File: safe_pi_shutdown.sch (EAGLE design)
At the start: 31 parts, among them U1 LTC2952CF

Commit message: prawie pierwsza wersja
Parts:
- added J1: 22-27-2021-02, con-molex:22-27-2021-02
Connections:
- removed net N$7: S1.2.1, U1.!PB
- new net N$5: J1-1.S, S1.2.1, S1.2.2, U1.!PB
- net GND: now also J1-2.S, X2.1; no longer X2.2
- net V1: now also X2.2; no longer X2.1
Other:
- moved on the sheet: X2
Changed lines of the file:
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@@
 <?xml version="1.0" encoding="utf-8"?>
 <!DOCTYPE eagle SYSTEM "eagle.dtd">
-<eagle version="6.5.0">
+<eagle version="6.6.0">
 <drawing>
 <settings>
@@
 <classes>
 <class number="0" name="default" width="0.2032" drill="0.6096">
-<clearance class="0" value="0.2032"/>
+<clearance class="0" value="0.205"/>
 </class>
 <class number="1" name="VCC" width="0.508" drill="0.6096">
-<clearance class="1" value="0.2032"/>
+<clearance class="0" value="0.205"/>
+<clearance class="1" value="0.205"/>
 </class>
 </classes>
@@
 <part name="U$2" library="mcp73831" deviceset="MCP73831" device=""/>
 <part name="SUPPLY14" library="supply2" deviceset="GND" device=""/>
+<part name="J1" library="con-molex" deviceset="22-?-02" device="27-2021"/>
 </parts>
 <sheets>
@@
 <instance part="SUPPLY3" gate="GND" x="38.1" y="154.94" rot="R180"/>
 <instance part="SUPPLY6" gate="GND" x="50.8" y="121.92"/>
-<instance part="X2" gate="G$1" x="25.4" y="127"/>
+<instance part="X2" gate="G$1" x="27.94" y="124.46" rot="MR180"/>
 <instance part="C7" gate="G$1" x="162.56" y="144.78"/>
 <instance part="C8" gate="G$1" x="220.98" y="160.02"/>
@@
 <instance part="U$2" gate="G$1" x="22.86" y="139.7" rot="MR180"/>
 <instance part="SUPPLY14" gate="GND" x="10.16" y="124.46"/>
+<instance part="J1" gate="-1" x="91.44" y="81.28"/>
+<instance part="J1" gate="-2" x="91.44" y="78.74"/>
 </instances>
 <busses>
@@
 <pinref part="SUPPLY6" gate="GND" pin="GND"/>
 <wire x1="50.8" y1="127" x2="50.8" y2="124.46" width="0.1524" layer="91"/>
-<pinref part="X2" gate="G$1" pin="2"/>
-<wire x1="33.02" y1="124.46" x2="50.8" y2="124.46" width="0.1524" layer="91"/>
+<pinref part="X2" gate="G$1" pin="1"/>
+<wire x1="35.56" y1="124.46" x2="50.8" y2="124.46" width="0.1524" layer="91"/>
 <junction x="50.8" y="124.46"/>
 </segment>
@@
 <junction x="68.58" y="88.9"/>
 <junction x="68.58" y="86.36"/>
+<wire x1="88.9" y1="78.74" x2="73.66" y2="78.74" width="0.1524" layer="91"/>
+<wire x1="73.66" y1="78.74" x2="73.66" y2="86.36" width="0.1524" layer="91"/>
+<junction x="73.66" y="86.36"/>
+<pinref part="J1" gate="-2" pin="S"/>
 </segment>
 <segment>
@@
 <wire x1="60.96" y1="104.14" x2="60.96" y2="106.68" width="0.1524" layer="91"/>
 <wire x1="60.96" y1="106.68" x2="68.58" y2="106.68" width="0.1524" layer="91"/>
-</segment>
-</net>
-<net name="N$7" class="0">
-<segment>
-<wire x1="96.52" y1="101.6" x2="86.36" y2="101.6" width="0.1524" layer="91"/>
-<pinref part="U1" gate="G$1" pin="!PB"/>
-<wire x1="86.36" y1="101.6" x2="86.36" y2="91.44" width="0.1524" layer="91"/>
-<pinref part="S1" gate="G$1" pin="2.1"/>
 </segment>
 </net>
@@
 <pinref part="C5" gate="G$1" pin="1"/>
 <wire x1="50.8" y1="139.7" x2="50.8" y2="137.16" width="0.1524" layer="91"/>
-<pinref part="X2" gate="G$1" pin="1"/>
 <wire x1="50.8" y1="137.16" x2="50.8" y2="134.62" width="0.1524" layer="91"/>
-<wire x1="33.02" y1="127" x2="40.64" y2="127" width="0.1524" layer="91"/>
 <pinref part="U$2" gate="G$1" pin="VBAT"/>
 <wire x1="33.02" y1="134.62" x2="40.64" y2="134.62" width="0.1524" layer="91"/>
@@
 <pinref part="U1" gate="G$1" pin="V1"/>
 <wire x1="78.74" y1="119.38" x2="96.52" y2="119.38" width="0.1524" layer="91"/>
+<pinref part="X2" gate="G$1" pin="2"/>
+<wire x1="35.56" y1="127" x2="40.64" y2="127" width="0.1524" layer="91"/>
 </segment>
 </net>
@@
 </segment>
 </net>
+<net name="N$5" class="0">
+<segment>
+<pinref part="S1" gate="G$1" pin="2.2"/>
+<wire x1="88.9" y1="81.28" x2="86.36" y2="81.28" width="0.1524" layer="91"/>
+<wire x1="86.36" y1="81.28" x2="86.36" y2="88.9" width="0.1524" layer="91"/>
+<wire x1="96.52" y1="101.6" x2="86.36" y2="101.6" width="0.1524" layer="91"/>
+<pinref part="U1" gate="G$1" pin="!PB"/>
+<wire x1="86.36" y1="101.6" x2="86.36" y2="91.44" width="0.1524" layer="91"/>
+<pinref part="S1" gate="G$1" pin="2.1"/>
+<wire x1="86.36" y1="88.9" x2="86.36" y2="91.44" width="0.1524" layer="91"/>
+<junction x="86.36" y="88.9"/>
+<junction x="86.36" y="91.44"/>
+<pinref part="J1" gate="-1" pin="S"/>
+</segment>
+</net>

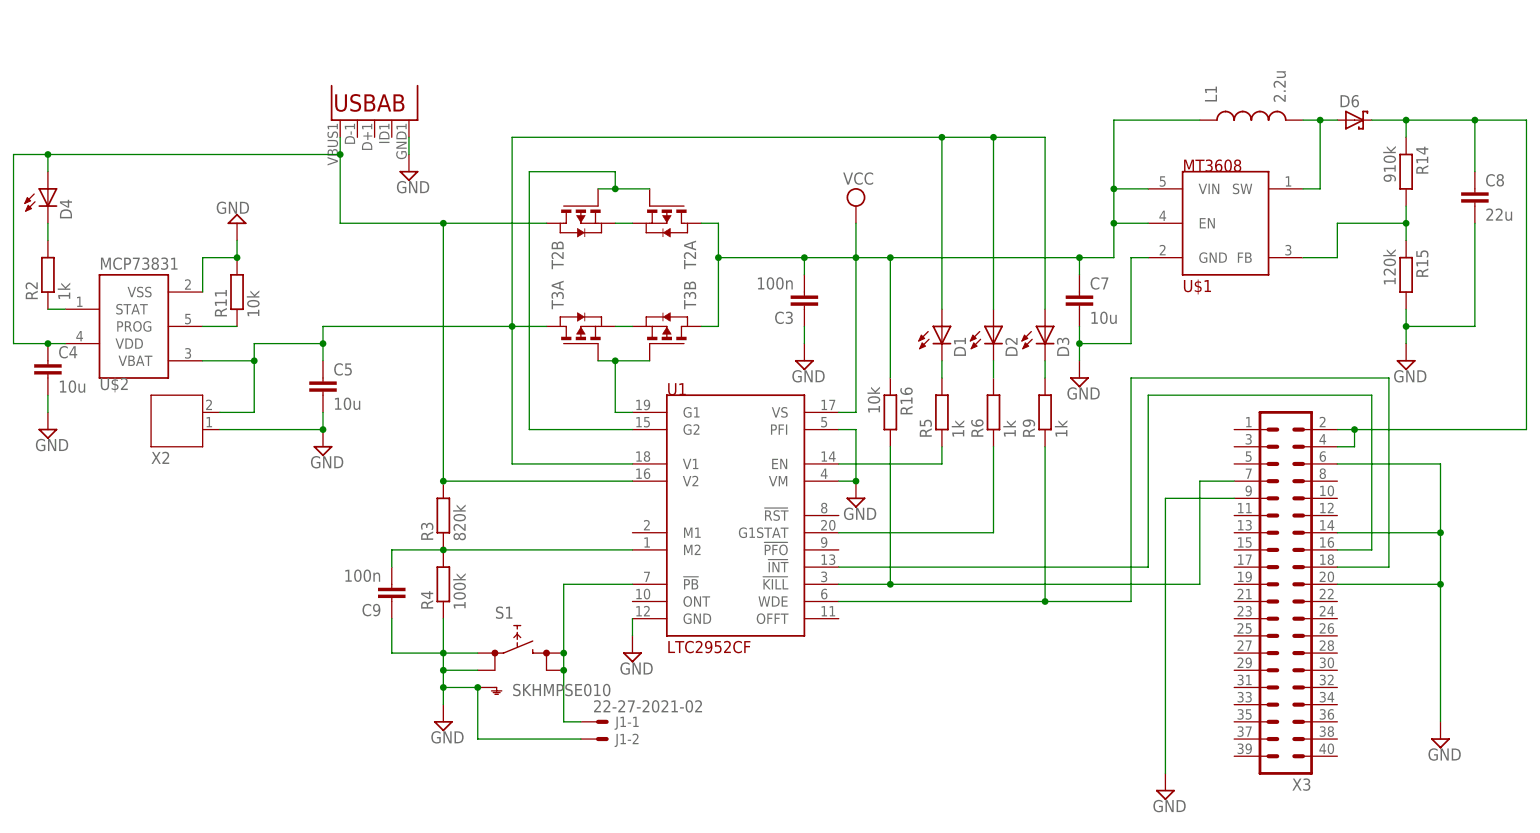
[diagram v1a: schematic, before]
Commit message: rozmieszczenie nazw na layaoucie
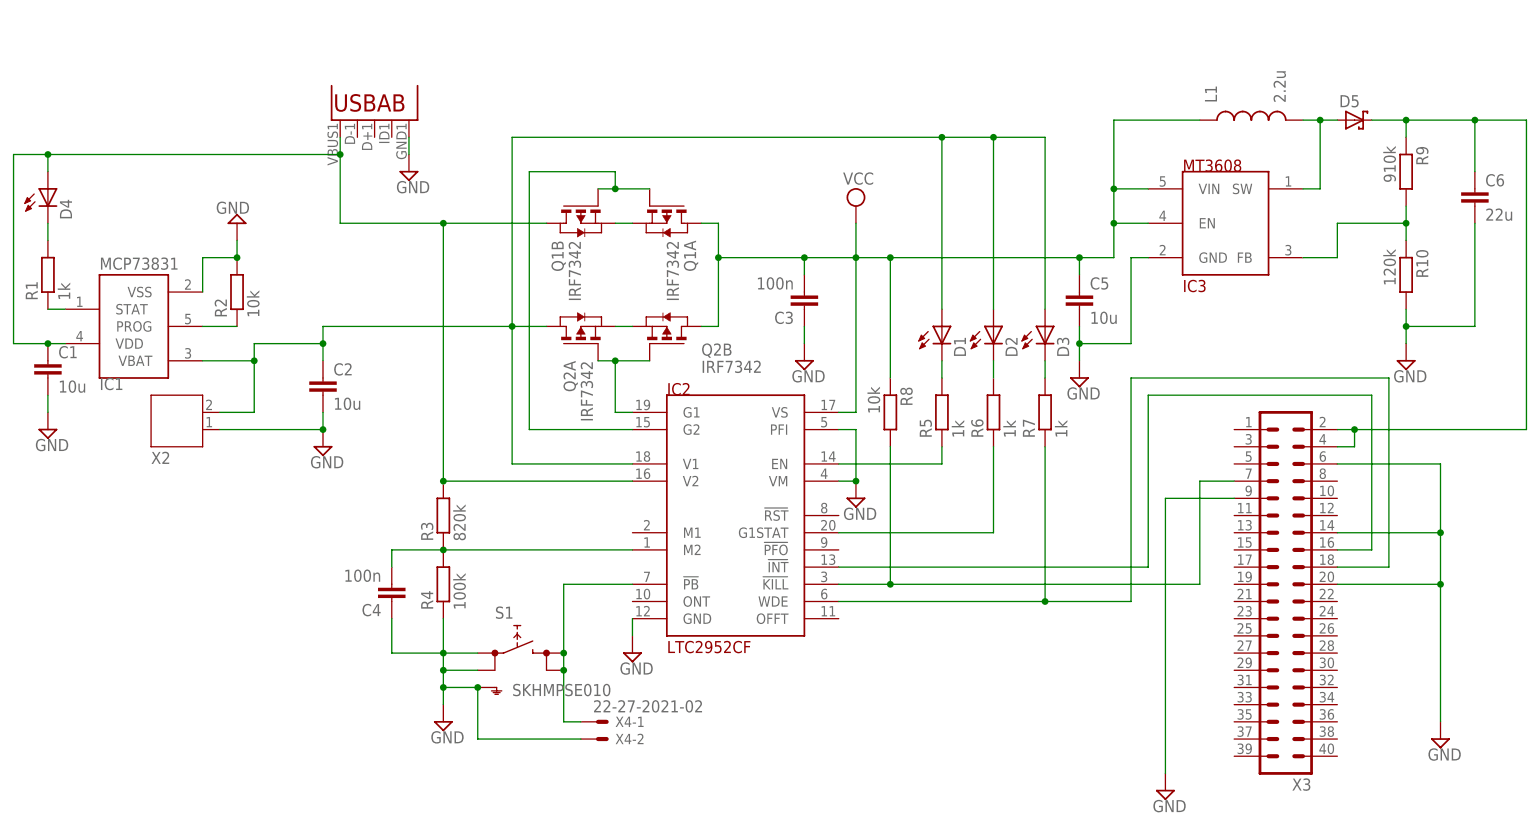
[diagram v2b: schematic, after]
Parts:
- removed C7: 10u, rcl:C-EUC0603
- removed C9: 100n, rcl:C-EUC0402
- removed R11: 10k, rcl:R-EU_R0603
- removed R14: 910k, rcl:R-EU_R0603
- added C1, C2: 10u, rcl:C-EUC0603
- added R1, R7: 1k, rcl:R-EU_R0603
- C4: value 10u -> 100n; device rcl:C-EUC0603 -> rcl:C-EUC0402
- Q1, Q2: value (none) -> IRF7342
- R2: value 1k -> 10k
- R9: value 1k -> 910k
- renumbered C8 to C6, D6 to D5, J1 to X4, R15 to R10, R16 to R8, T2 to Q1, T3 to Q2, U$1 to IC3, U$2 to IC1, U1 to IC2
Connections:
- net GND: now also C1.2, C2.2, C4.1, R2.2; no longer C4.2, C7.2, C9.1, R11.2
- net N$14: now also R2.1; no longer R11.1
- net N$15: now also R7.2; no longer R9.2
- net N$18: now also R7.1; no longer R9.1
- net N$21: now also R9.2; no longer R14.2
- net N$23: now also R1.1; no longer R2.1
- net N$4: now also R9.1; no longer R14.1
- net N$6: now also R1.2; no longer R2.2
- net N$8: now also C4.2; no longer C9.2
- net V1: now also C2.1; no longer C5.1
- net V2: now also C1.1; no longer C4.1
- net VCC: now also C5.1; no longer C7.1
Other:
- moved on the sheet: C4, C5, R2, R9

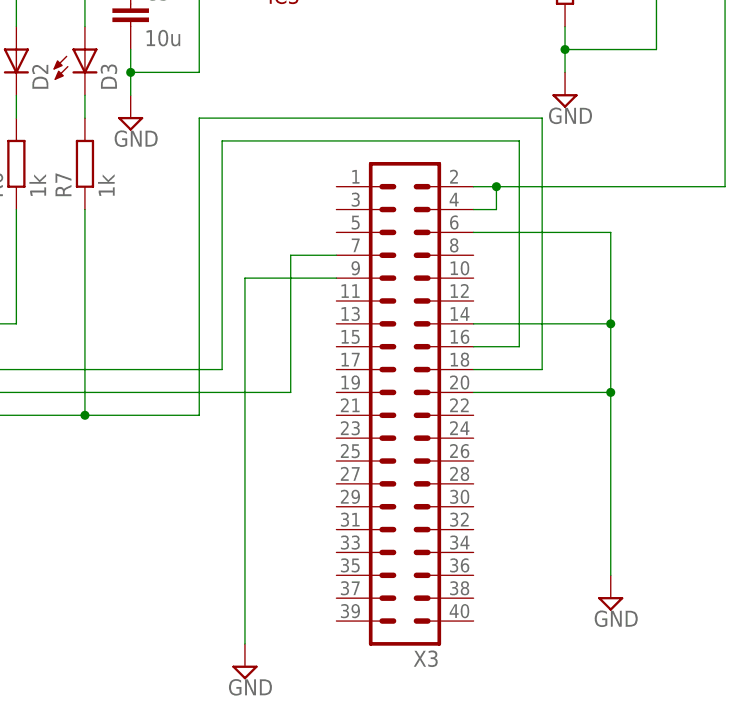
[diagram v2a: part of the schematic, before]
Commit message: dostosowanie do nanopi zero (pozycja konektora)
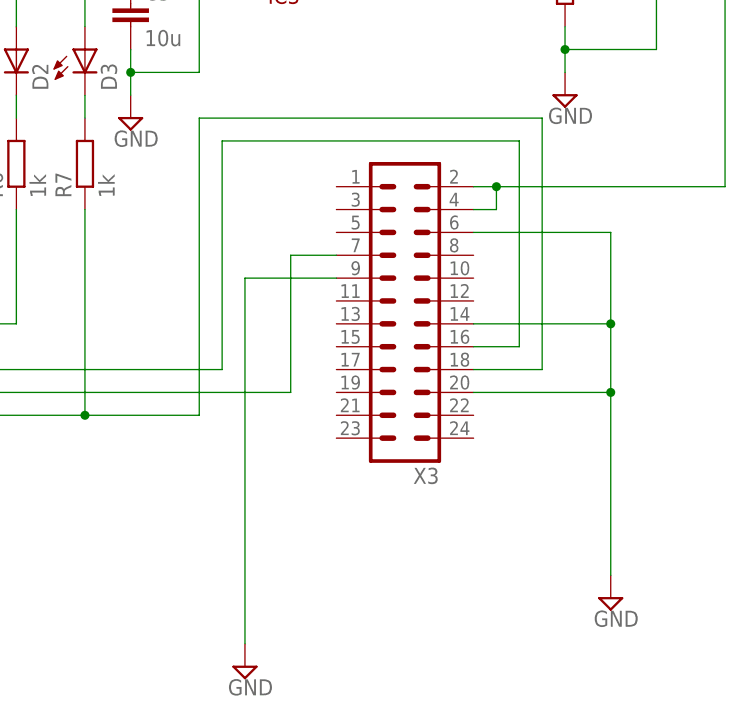
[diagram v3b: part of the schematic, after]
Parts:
- X3: device con-lstb:MA20-2 -> con-lstb:MA12-2
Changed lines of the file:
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@@
 <part name="R6" library="rcl" deviceset="R-EU_" device="R0603" value="1k"/>
 <part name="SUPPLY2" library="supply2" deviceset="VCC" device=""/>
-<part name="X3" library="con-lstb" deviceset="MA20-2" device=""/>
 <part name="IC2" library="ltc2952" deviceset="LTC2952CF" device=""/>
 <part name="X1" library="MicroUSB" deviceset="USB" device="&quot;&quot;"/>
@@
 <part name="SUPPLY14" library="supply2" deviceset="GND" device=""/>
 <part name="X4" library="con-molex" deviceset="22-?-02" device="27-2021"/>
+<part name="X3" library="con-lstb" deviceset="MA12-2" device=""/>
 </parts>
 <sheets>
@@
 <instance part="R6" gate="G$1" x="149.86" y="127" rot="R90"/>
 <instance part="SUPPLY2" gate="G$1" x="129.54" y="157.48"/>
-<instance part="X3" gate="G$1" x="193.04" y="99.06" rot="R180"/>
 <instance part="IC2" gate="G$1" x="111.76" y="111.76"/>
 <instance part="X1" gate="G$1" x="58.42" y="172.72" rot="MR90"/>
@@
 <instance part="X4" gate="-1" x="91.44" y="81.28"/>
 <instance part="X4" gate="-2" x="91.44" y="78.74"/>
+<instance part="X3" gate="1" x="193.04" y="111.76" rot="R180"/>
 </instances>
 <busses>
@@
 </segment>
 <segment>
-<pinref part="X3" gate="G$1" pin="9"/>
 <wire x1="185.42" y1="114.3" x2="175.26" y2="114.3" width="0.1524" layer="91"/>
 <wire x1="175.26" y1="114.3" x2="175.26" y2="73.66" width="0.1524" layer="91"/>
 <pinref part="SUPPLY13" gate="GND" pin="GND"/>
-</segment>
-<segment>
-<pinref part="X3" gate="G$1" pin="6"/>
+<pinref part="X3" gate="1" pin="9"/>
+</segment>
+<segment>
 <wire x1="200.66" y1="119.38" x2="215.9" y2="119.38" width="0.1524" layer="91"/>
 <wire x1="215.9" y1="119.38" x2="215.9" y2="109.22" width="0.1524" layer="91"/>
-<pinref part="X3" gate="G$1" pin="14"/>
 <wire x1="215.9" y1="109.22" x2="200.66" y2="109.22" width="0.1524" layer="91"/>
 <wire x1="215.9" y1="109.22" x2="215.9" y2="101.6" width="0.1524" layer="91"/>
-<pinref part="X3" gate="G$1" pin="20"/>
 <wire x1="215.9" y1="101.6" x2="200.66" y2="101.6" width="0.1524" layer="91"/>
 <wire x1="215.9" y1="101.6" x2="215.9" y2="81.28" width="0.1524" layer="91"/>
@@
 <junction x="215.9" y="101.6"/>
 <pinref part="SUPPLY7" gate="GND" pin="GND"/>
+<pinref part="X3" gate="1" pin="6"/>
+<pinref part="X3" gate="1" pin="14"/>
+<pinref part="X3" gate="1" pin="20"/>
 </segment>
 <segment>
@@
 <wire x1="134.62" y1="101.6" x2="180.34" y2="101.6" width="0.1524" layer="91"/>
 <wire x1="180.34" y1="101.6" x2="180.34" y2="116.84" width="0.1524" layer="91"/>
-<pinref part="X3" gate="G$1" pin="7"/>
 <wire x1="180.34" y1="116.84" x2="185.42" y2="116.84" width="0.1524" layer="91"/>
 <pinref part="R8" gate="G$1" pin="2"/>
 <wire x1="134.62" y1="121.92" x2="134.62" y2="101.6" width="0.1524" layer="91"/>
 <junction x="134.62" y="101.6"/>
+<pinref part="X3" gate="1" pin="7"/>
 </segment>
 </net>
@@
 <wire x1="170.18" y1="132.08" x2="208.28" y2="132.08" width="0.1524" layer="91"/>
 <wire x1="208.28" y1="132.08" x2="208.28" y2="104.14" width="0.1524" layer="91"/>
-<pinref part="X3" gate="G$1" pin="18"/>
 <wire x1="208.28" y1="104.14" x2="200.66" y2="104.14" width="0.1524" layer="91"/>
 <junction x="157.48" y="99.06"/>
+<pinref part="X3" gate="1" pin="18"/>
 </segment>
 </net>
@@
 <wire x1="220.98" y1="170.18" x2="228.6" y2="170.18" width="0.1524" layer="91"/>
 <wire x1="228.6" y1="170.18" x2="228.6" y2="124.46" width="0.1524" layer="91"/>
-<pinref part="X3" gate="G$1" pin="2"/>
 <wire x1="200.66" y1="124.46" x2="203.2" y2="124.46" width="0.1524" layer="91"/>
 <wire x1="203.2" y1="121.92" x2="203.2" y2="124.46" width="0.1524" layer="91"/>
-<pinref part="X3" gate="G$1" pin="4"/>
 <wire x1="200.66" y1="121.92" x2="203.2" y2="121.92" width="0.1524" layer="91"/>
 <wire x1="228.6" y1="124.46" x2="203.2" y2="124.46" width="0.1524" layer="91"/>
 <junction x="203.2" y="124.46"/>
 <junction x="220.98" y="170.18"/>
+<pinref part="X3" gate="1" pin="2"/>
+<pinref part="X3" gate="1" pin="4"/>
 </segment>
 </net>
@@
 <wire x1="172.72" y1="129.54" x2="205.74" y2="129.54" width="0.1524" layer="91"/>
 <wire x1="205.74" y1="129.54" x2="205.74" y2="106.68" width="0.1524" layer="91"/>
-<pinref part="X3" gate="G$1" pin="16"/>
 <wire x1="205.74" y1="106.68" x2="200.66" y2="106.68" width="0.1524" layer="91"/>
-</segment>
-</net>
+<pinref part="X3" gate="1" pin="16"/>
+</segment>
+</net>
